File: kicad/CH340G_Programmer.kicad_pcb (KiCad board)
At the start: 2 copper layers, 37 x 18.5 mm, 19 parts, among them J1 USB_B_Micro, J2 PROG, Q1 MMBT2222A 1P, Q2 MMBT2222A 1P, U1 AMS1117-3.3, U2 CH340G, Y1 12MHz

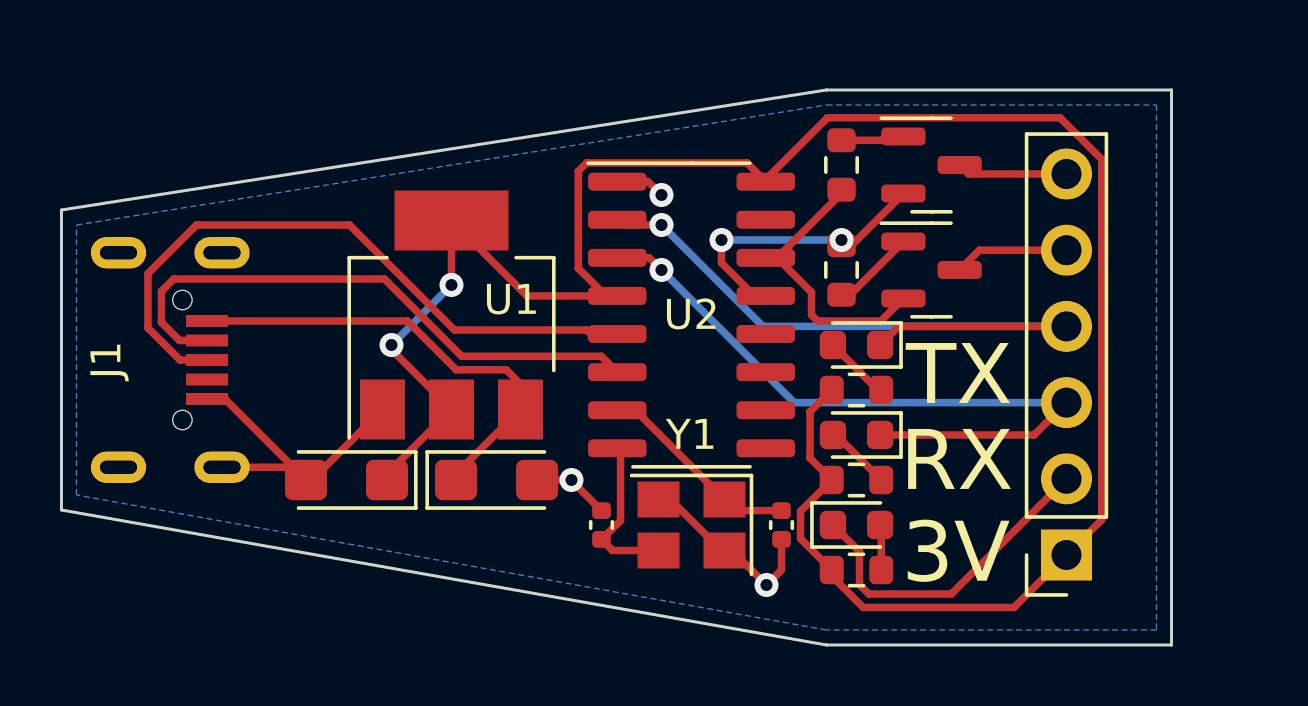
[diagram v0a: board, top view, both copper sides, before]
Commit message: Added jumper to allow choice of power to target or not.  Also added LED to indicate additional power rail
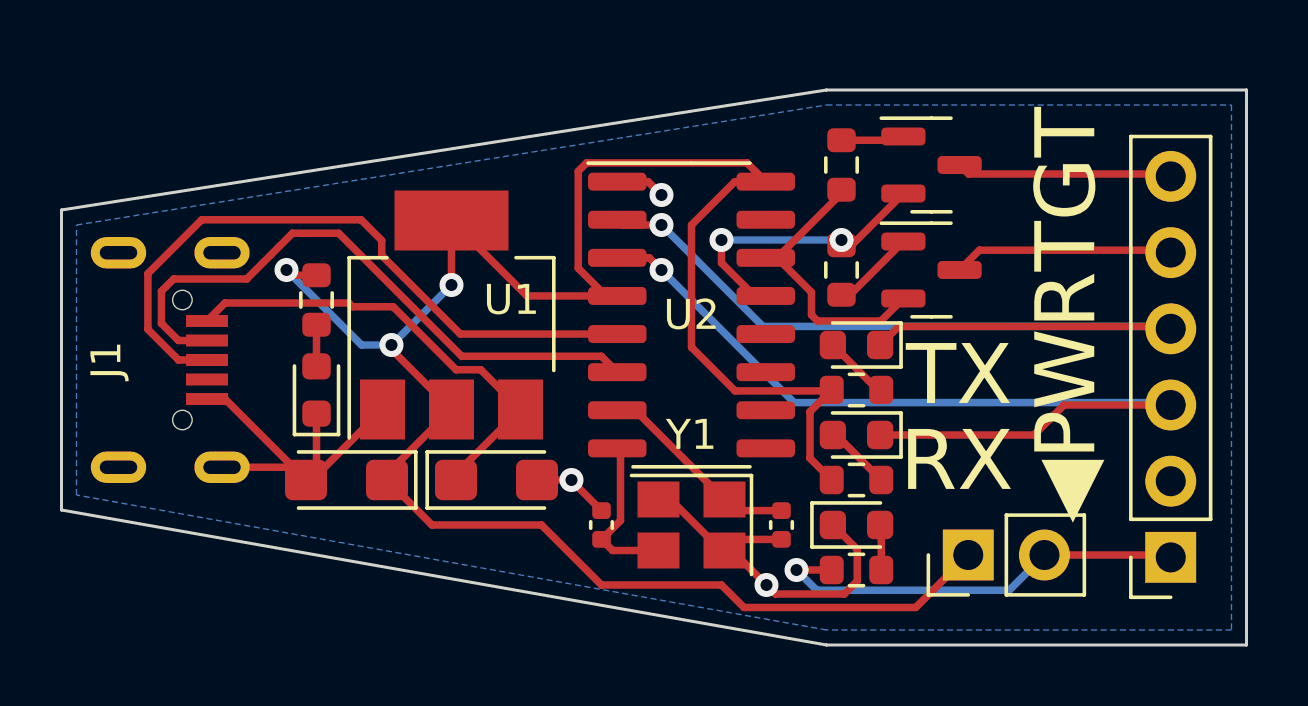
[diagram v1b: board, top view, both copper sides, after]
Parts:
- added D4: RED, LED_SMD:LED_0603_1608Metric, F.Cu at (150.0, 97.0)
- added JP1: PWR_TGT, Connector_PinHeader_2.54mm:PinHeader_1x02_P2.54mm_Vertical, F.Cu at (171.7, 102.5)
- added R6: 330, Resistor_SMD:R_0603_1608Metric, F.Cu at (150.0, 94.0)
- moved J2 3.48 mm to (178.5, 102.6)
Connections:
- J2 pad 1: +3V3 -> Net-(R3-Pad1)
- R3 pad 1: +3V3 -> Net-(R3-Pad1)
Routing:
- net Net-(R3-Pad1): track 0.00 -> 14.4 mm, vias 0 -> 1
- net TXDO: track 22.9 -> 29.7 mm
- net RXDI: track 23.6 -> 30.4 mm
- net RESET: track 3.84 -> 7.21 mm
- net BOOT: track 3.69 -> 7.06 mm
- net GND: track 32.6 -> 29.9 mm
- net Net-(D4-Pad2): track 0.00 -> 1.39 mm
- net Net-(J1-Pad2): track 19.5 -> 20.7 mm
- net +3V3: track 72.3 -> 72.8 mm, vias 2 -> 3
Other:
- board size 37 x 18.5 mm -> 39.5 x 18.5 mm
- board text added: "◀PWRTGT"
- board text removed: "3V"
